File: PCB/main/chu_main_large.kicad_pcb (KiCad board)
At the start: 2 copper layers, 500 x 100 mm, 125 parts, among them K1 ChuKeyLarge, K10 Conn_01x01_Female, K11 Conn_01x01_Female, K12 Conn_01x01_Female, K13 Conn_01x01_Female, K14 Conn_01x01_Female, K15 Conn_01x01_Female, K16 Conn_01x01_Female, K17 Conn_01x01_Female, K18 Conn_01x01_Female, K19 Conn_01x01_Female, K2 Conn_01x01_Female, K20 Conn_01x01_Female, K21 Conn_01x01_Female, K22 Conn_01x01_Female, K23 Conn_01x01_Female, K24 Conn_01x01_Female, K25 Conn_01x01_Female, K26 Conn_01x01_Female, K27 Conn_01x01_Female, K28 Conn_01x01_Female, K29 Conn_01x01_Female, K3 Conn_01x01_Female, K30 Conn_01x01_Female, K31 Conn_01x01_Female, K32 Conn_01x01_Female, K4 Conn_01x01_Female, K5 Conn_01x01_Female, K6 Conn_01x01_Female, K7 Conn_01x01_Female, K8 Conn_01x01_Female, K9 Conn_01x01_Female, SW1 SPST_EVQP4, SW2 SPST_EVQP4, SW3 SPST_EVQP4, U0 ChuAcrylicLarge, U1 PiPico_No_SWD, U2 PCA9548APW, U3 MPR121QR2, U4 MPR121QR2, U5 MPR121QR2, U6 MPR121QR2, X1 GP2Y0E03_REAL, X2 GP2Y0E03_REAL, X3 GP2Y0E03_REAL, X4 GP2Y0E03_REAL, X5 GP2Y0E03_REAL

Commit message: improve touch based on online infos
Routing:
- net GND: track 2089.7 -> 2769.7 mm
- net /SCL_4: track 152.6 -> 156.8 mm
- net /SCL: track 566.6 -> 568.6 mm
- net /SCL_5: track 253.5 -> 255.4 mm
- net /SDA: track 552.4 -> 554.1 mm
- net /SCL_3: track 74.6 -> 72.9 mm
- net /SDA_3: track 72.4 -> 71.0 mm
- net +3V3: track 940.5 -> 941.3 mm
- net +5V: track 1254.7 -> 1253.9 mm
- net Net-(D32-Out): track 127.8 -> 127.1 mm
- net /SDA_5: track 254.5 -> 255.0 mm
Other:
- board text added: "Chu Pico V1.61 Large Rev V1.01"
- board text removed: "Chu Pico V1.61 Large Rev V1.00"

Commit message: solder improvements, started case
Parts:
- moved JT2 20.0 mm to (85.7, 69.3), turned to 90 degrees
- moved JT1 18.1 mm to (527.7, 121.6)
- moved U0 0.25 mm to (291.2, 107.8)
- moved X2 0.10 mm to (133.9, 151.3)
- moved X3 0.10 mm to (300.4, 151.3)
- moved X4 0.10 mm to (447.4, 151.3)
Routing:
- net GND: track 2769.7 -> 2871.7 mm, vias 37 -> 36
- net Net-(JT1-Data): track 572.0 -> 614.4 mm
- net Net-(JT1-A): track 564.9 -> 605.5 mm
- net Net-(JT1-B): track 560.7 -> 598.8 mm
- net Net-(JT1-C): track 556.5 -> 593.0 mm
- net Net-(JT2-Data): track 62.6 -> 81.1 mm
- net +3V3: track 941.3 -> 953.0 mm
- net Net-(K9-Pin_1): track 91.6 -> 102.1 mm
- net Net-(K25-Pin_1): track 93.6 -> 102.9 mm
- net Net-(K17-Pin_1): track 92.8 -> 100.2 mm
- net Net-(K11-Pin_1): track 66.0 -> 72.4 mm
- net Net-(K19-Pin_1): track 61.6 -> 67.1 mm
- net Net-(K31-Pin_1): track 73.5 -> 78.6 mm
- net Net-(K3-Pin_1): track 62.3 -> 65.4 mm
- net Net-(K13-Pin_1): track 56.3 -> 58.4 mm
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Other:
- board text added: "Chu Pico V1.61 Large Rev V1.02"
- board text removed: "Chu Pico V1.61 Large Rev V1.01"

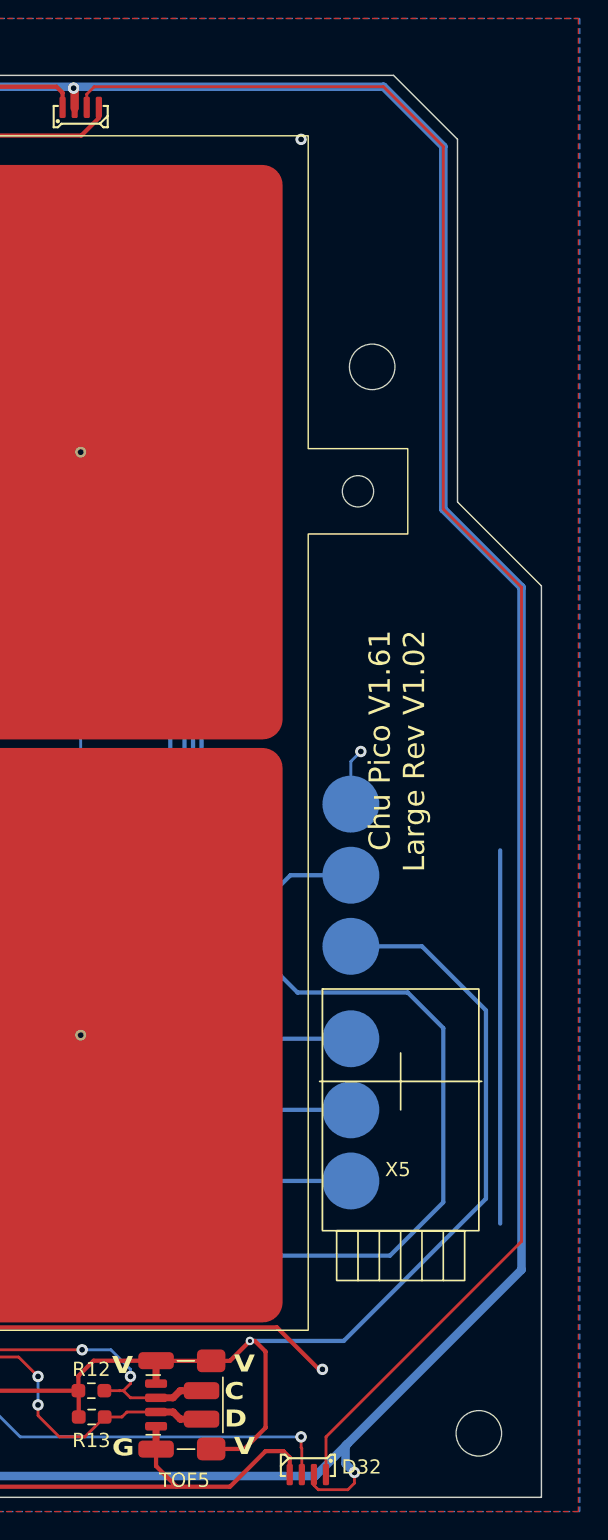
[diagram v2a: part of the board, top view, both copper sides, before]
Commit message: fix LED orientation
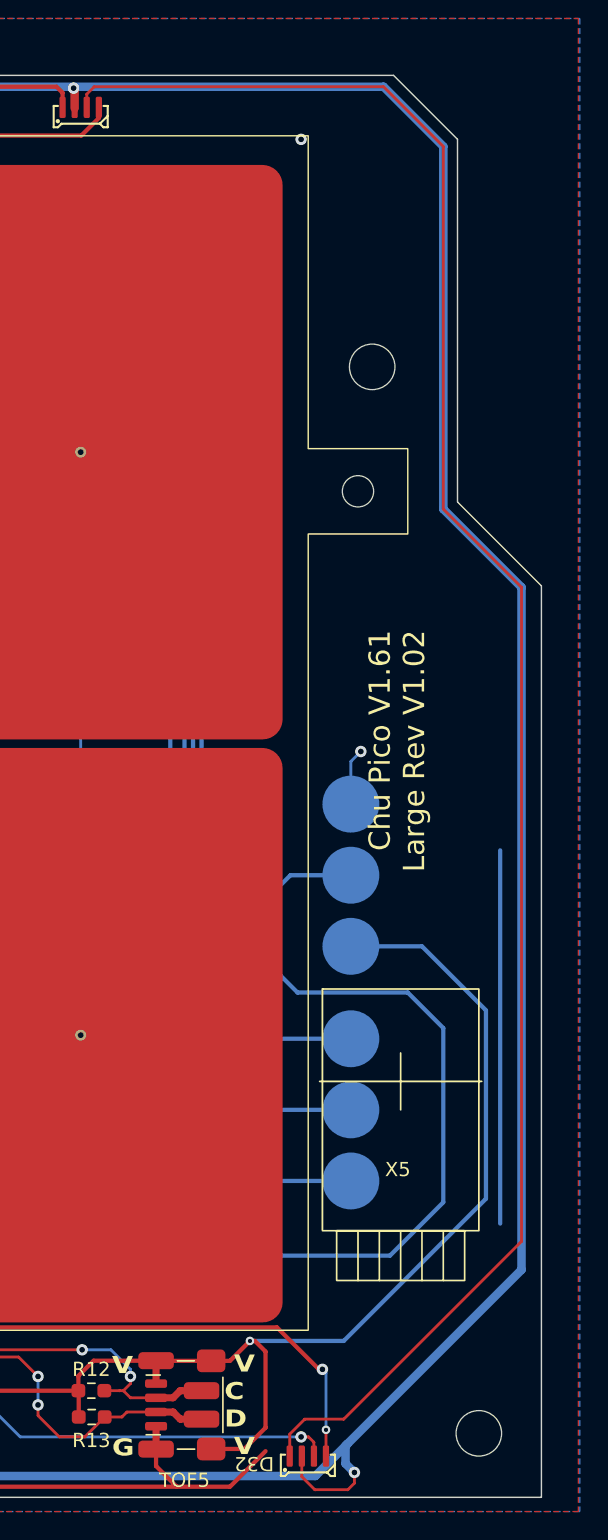
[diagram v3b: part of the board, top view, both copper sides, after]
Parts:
- turned D32 to 180 degrees
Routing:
- net GND: track 2871.7 -> 2874.8 mm, vias 36 -> 37
- net +5V: track 1253.9 -> 1255.7 mm
- net Net-(D31-Out): track 129.3 -> 130.7 mm
- net Net-(D32-Out): track 127.1 -> 126.5 mm
